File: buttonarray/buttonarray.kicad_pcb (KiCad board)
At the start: 2 copper layers, 0 parts

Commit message: add: component placement for numpad
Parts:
- added C1: 33pF, Capacitor_SMD:C_0201_0603Metric_Pad0.64x0.40mm_HandSolder, B.Cu at (55.9, 104.1)
- added C2: 1000uF, Capacitor_THT:CP_Radial_D13.0mm_P5.00mm, B.Cu at (50.8, 114.3)
- added C3: 100 uF, Capacitor_THT:CP_Radial_D6.3mm_P2.50mm, B.Cu at (76.2, 48.3)
- added C4: 330uF, Capacitor_THT:CP_Radial_D10.0mm_P5.00mm, B.Cu at (66.0, 50.8)
- added D1: 1N5819, Diode_THT:D_DO-41_SOD81_P10.16mm_Horizontal, B.Cu at (83.8, 53.3)
- added D10: 1N5819, Diode_THT:D_DO-41_SOD81_P10.16mm_Horizontal, B.Cu at (104.1, 94.0)
- added D11: 1N5819, Diode_THT:D_DO-41_SOD81_P10.16mm_Horizontal, B.Cu at (124.5, 94.0)
- added D12: 1N5819, Diode_THT:D_DO-41_SOD81_P10.16mm_Horizontal, B.Cu at (144.8, 94.0)
- added D13: 1N5819, Diode_THT:D_DO-41_SOD81_P10.16mm_Horizontal, B.Cu at (83.8, 114.3)
- added D14: 1N5819, Diode_THT:D_DO-41_SOD81_P10.16mm_Horizontal, B.Cu at (104.1, 114.3)
- added D15: 1N5819, Diode_THT:D_DO-41_SOD81_P10.16mm_Horizontal, B.Cu at (124.5, 114.3)
- added D16: 1N5819, Diode_THT:D_DO-41_SOD81_P10.16mm_Horizontal, B.Cu at (147.3, 114.3)
- added D17: 1N5819, Diode_THT:D_DO-41_SOD81_P10.16mm_Horizontal, B.Cu at (61.0, 40.6)
- added D2: 1N5819, Diode_THT:D_DO-41_SOD81_P10.16mm_Horizontal, B.Cu at (104.1, 53.3)
- added D3: 1N5819, Diode_THT:D_DO-41_SOD81_P10.16mm_Horizontal, B.Cu at (124.5, 53.3)
- added D4: 1N5819, Diode_THT:D_DO-41_SOD81_P10.16mm_Horizontal, B.Cu at (144.8, 53.3)
- added D5: 1N5819, Diode_THT:D_DO-41_SOD81_P10.16mm_Horizontal, B.Cu at (83.8, 73.7)
- added D6: 1N5819, Diode_THT:D_DO-41_SOD81_P10.16mm_Horizontal, B.Cu at (104.1, 73.7)
- added D7: 1N5819, Diode_THT:D_DO-41_SOD81_P10.16mm_Horizontal, B.Cu at (124.5, 73.7)
- added D8: 1N5819, Diode_THT:D_DO-41_SOD81_P10.16mm_Horizontal, B.Cu at (144.8, 73.7)
- added D9: 1N5819, Diode_THT:D_DO-41_SOD81_P10.16mm_Horizontal, B.Cu at (83.8, 94.0)
- added GPIOEXP1: mcp23016, Mission_DMX_Footprint_Library:mcp23016, F.Cu at (62.2, 118.1)
- added J1: CtrlPins, Connector_IDC:IDC-Header_2x08_P2.54mm_Latch_Vertical, B.Cu at (53.3, 73.7)
- added L1: 330 uH, Inductor_SMD:L_Fastron_PISN_Handsoldering, B.Cu at (71.1, 33.0)
- added Q1: 2N2219, Package_TO_SOT_THT:TO-39-3, B.Cu at (157.5, 33.0)
- added Q10: 2N2219, Package_TO_SOT_THT:TO-39-3, B.Cu at (96.5, 33.0)
- added Q11: 2N2219, Package_TO_SOT_THT:TO-39-3, B.Cu at (170.2, 71.1)
- added Q12: 2N2219, Package_TO_SOT_THT:TO-39-3, B.Cu at (170.3, 114.3)
- added Q13: 2N2219, Package_TO_SOT_THT:TO-39-3, B.Cu at (116.8, 33.0)
- added Q14: 2N2219, Package_TO_SOT_THT:TO-39-3, B.Cu at (170.2, 50.8)
- added Q15: 2N2219, Package_TO_SOT_THT:TO-39-3, B.Cu at (94.0, 124.5)
- added Q16: 2N2219, Package_TO_SOT_THT:TO-39-3, B.Cu at (137.2, 33.0)
- added Q2: 2N2219, Package_TO_SOT_THT:TO-39-3, B.Cu at (78.7, 88.9)
- added Q3: 2N2219, Package_TO_SOT_THT:TO-39-3, B.Cu at (114.3, 124.5)
- added Q4: 2N2219, Package_TO_SOT_THT:TO-39-3, B.Cu at (78.7, 58.4)
- added Q5: 2N2219, Package_TO_SOT_THT:TO-39-3, B.Cu at (78.7, 106.7)
- added Q6: 2N2219, Package_TO_SOT_THT:TO-39-3, B.Cu at (137.2, 124.5)
- added Q7: 2N2219, Package_TO_SOT_THT:TO-39-3, B.Cu at (78.7, 76.2)
- added Q8: 2N2219, Package_TO_SOT_THT:TO-39-3, B.Cu at (170.2, 91.4)
- added Q9: 2N2219, Package_TO_SOT_THT:TO-39-3, B.Cu at (154.9, 124.5)
- added R1: 10K, Resistor_SMD:R_0805_2012Metric_Pad1.20x1.40mm_HandSolder, B.Cu at (58.4, 99.1)
- added R10: 330 Ohm, Resistor_SMD:R_1206_3216Metric_Pad1.30x1.75mm_HandSolder, B.Cu at (104.1, 123.5)
- added R11: 3K, Resistor_SMD:R_1206_3216Metric_Pad1.30x1.75mm_HandSolder, B.Cu at (68.6, 61.0)
- added R12: 3K, Resistor_SMD:R_1206_3216Metric_Pad1.30x1.75mm_HandSolder, B.Cu at (78.7, 114.3)
- added R13: 3K, Resistor_SMD:R_1206_3216Metric_Pad1.30x1.75mm_HandSolder, B.Cu at (127.0, 127.0)
- added R14: 330 Ohm, Resistor_SMD:R_1206_3216Metric_Pad1.30x1.75mm_HandSolder, B.Cu at (76.2, 66.0)
- added R15: 330 Ohm, Resistor_SMD:R_1206_3216Metric_Pad1.30x1.75mm_HandSolder, B.Cu at (73.7, 116.8)
- added R16: 330 Ohm, Resistor_SMD:R_1206_3216Metric_Pad1.30x1.75mm_HandSolder, B.Cu at (124.5, 121.9)
- added R17: 3K, Resistor_SMD:R_1206_3216Metric_Pad1.30x1.75mm_HandSolder, B.Cu at (68.6, 78.7)
- added R18: 3K, Resistor_SMD:R_1206_3216Metric_Pad1.30x1.75mm_HandSolder, B.Cu at (170.2, 99.1)
- added R19: 3K, Resistor_SMD:R_1206_3216Metric_Pad1.30x1.75mm_HandSolder, B.Cu at (144.8, 127.0)
- added R2: 10K, Resistor_SMD:R_0805_2012Metric_Pad1.20x1.40mm_HandSolder, B.Cu at (53.3, 99.1)
- added R20: 330 Ohm, Resistor_SMD:R_1206_3216Metric_Pad1.30x1.75mm_HandSolder, B.Cu at (68.6, 68.6)
- added R21: 330 Ohm, Resistor_SMD:R_1206_3216Metric_Pad1.30x1.75mm_HandSolder, B.Cu at (166.7, 83.8)
- added R22: 330 Ohm, Resistor_SMD:R_1206_3216Metric_Pad1.30x1.75mm_HandSolder, B.Cu at (142.2, 120.9)
- added R23: 3K, Resistor_SMD:R_1206_3216Metric_Pad1.30x1.75mm_HandSolder, B.Cu at (86.4, 35.6)
- added R24: 330 Ohm, Resistor_SMD:R_1206_3216Metric_Pad1.30x1.75mm_HandSolder, B.Cu at (83.8, 30.5)
- added R25: 3K, Resistor_SMD:R_1206_3216Metric_Pad1.30x1.75mm_HandSolder, B.Cu at (167.6, 78.7)
- added R26: 3K, Resistor_SMD:R_1206_3216Metric_Pad1.30x1.75mm_HandSolder, B.Cu at (167.7, 121.9)
- added R27: 330 Ohm, Resistor_SMD:R_1206_3216Metric_Pad1.30x1.75mm_HandSolder, B.Cu at (167.6, 63.5)
- added R28: 330 Ohm, Resistor_SMD:R_1206_3216Metric_Pad1.30x1.75mm_HandSolder, B.Cu at (167.7, 106.7)
- added R29: 3K, Resistor_SMD:R_1206_3216Metric_Pad1.30x1.75mm_HandSolder, B.Cu at (104.1, 30.5)
- added R3: 10K, Resistor_SMD:R_0805_2012Metric_Pad1.20x1.40mm_HandSolder, B.Cu at (48.3, 99.1)
- added R30: 330 Ohm, Resistor_SMD:R_1206_3216Metric_Pad1.30x1.75mm_HandSolder, B.Cu at (106.7, 34.6)
- added R31: 3K, Resistor_SMD:R_1206_3216Metric_Pad1.30x1.75mm_HandSolder, B.Cu at (167.6, 58.4)
- added R32: 3K, Resistor_SMD:R_1206_3216Metric_Pad1.30x1.75mm_HandSolder, B.Cu at (83.8, 125.5)
- added R33: 330 Ohm, Resistor_SMD:R_1206_3216Metric_Pad1.30x1.75mm_HandSolder, B.Cu at (167.6, 43.2)
- added R34: 330 Ohm, Resistor_SMD:R_1206_3216Metric_Pad1.30x1.75mm_HandSolder, B.Cu at (78.7, 121.9)
- added R35: 3K, Resistor_SMD:R_1206_3216Metric_Pad1.30x1.75mm_HandSolder, B.Cu at (124.5, 30.5)
- added R36: 330 Ohm, Resistor_SMD:R_1206_3216Metric_Pad1.30x1.75mm_HandSolder, B.Cu at (126.3, 35.6)
- added R4: 3.9K, Resistor_SMD:R_0603_1608Metric_Pad0.98x0.95mm_HandSolder, B.Cu at (50.8, 104.1)
- added R5: 3K, Resistor_SMD:R_1206_3216Metric_Pad1.30x1.75mm_HandSolder, B.Cu at (144.8, 30.5)
- added R6: 3K, Resistor_SMD:R_1206_3216Metric_Pad1.30x1.75mm_HandSolder, B.Cu at (78.7, 96.5)
- added R7: 3K, Resistor_SMD:R_1206_3216Metric_Pad1.30x1.75mm_HandSolder, B.Cu at (119.4, 124.5)
- added R8: 330 Ohm, Resistor_SMD:R_1206_3216Metric_Pad1.30x1.75mm_HandSolder, B.Cu at (147.3, 35.6)
- added R9: 330 Ohm, Resistor_SMD:R_1206_3216Metric_Pad1.30x1.75mm_HandSolder, B.Cu at (73.7, 99.1)
- added SW1: SW_Push_LED, Mission_DMX_Footprint_Library:MX-1.0u-LED, F.Cu at (94.0, 48.3)
- added SW10: SW_Push_LED, Mission_DMX_Footprint_Library:MX-1.0u-LED, F.Cu at (114.3, 88.9)
- added SW11: SW_Push_LED, Mission_DMX_Footprint_Library:MX-1.0u-LED, F.Cu at (134.6, 88.9)
- added SW12: SW_Push_LED, Mission_DMX_Footprint_Library:MX-1.0u-LED, F.Cu at (154.9, 88.9)
- added SW13: SW_Push_LED, Mission_DMX_Footprint_Library:MX-1.0u-LED, F.Cu at (94.0, 109.2)
- added SW14: SW_Push_LED, Mission_DMX_Footprint_Library:MX-1.0u-LED, F.Cu at (114.3, 109.2)
- added SW15: SW_Push_LED, Mission_DMX_Footprint_Library:MX-1.0u-LED, B.Cu at (134.6, 109.2)
- added SW16: SW_Push_LED, Mission_DMX_Footprint_Library:MX-1.0u-LED, F.Cu at (154.9, 109.2)
- added SW17: Addr_DIP_SW, Button_Switch_THT:SW_DIP_SPSTx03_Slide_9.78x9.8mm_W7.62mm_P2.54mm, F.Cu at (59.6, 94.0)
- added SW2: SW_Push_LED, Mission_DMX_Footprint_Library:MX-1.0u-LED, F.Cu at (114.3, 48.3)
- added SW3: SW_Push_LED, Mission_DMX_Footprint_Library:MX-1.0u-LED, F.Cu at (134.6, 48.3)
- added SW4: SW_Push_LED, Mission_DMX_Footprint_Library:MX-1.0u-LED, F.Cu at (154.9, 48.3)
- added SW5: SW_Push_LED, Mission_DMX_Footprint_Library:MX-1.0u-LED, F.Cu at (94.0, 68.6)
- added SW6: SW_Push_LED, Mission_DMX_Footprint_Library:MX-1.0u-LED, F.Cu at (114.3, 68.6)
- added SW7: SW_Push_LED, Mission_DMX_Footprint_Library:MX-1.0u-LED, F.Cu at (134.6, 68.6)
- added SW8: SW_Push_LED, Mission_DMX_Footprint_Library:MX-1.0u-LED, F.Cu at (154.9, 68.6)
- added SW9: SW_Push_LED, Mission_DMX_Footprint_Library:MX-1.0u-LED, F.Cu at (94.0, 88.9)
- added U1: LM2575-3.3BT, Package_TO_SOT_THT:TO-220-5_Vertical, B.Cu at (55.9, 33.0)

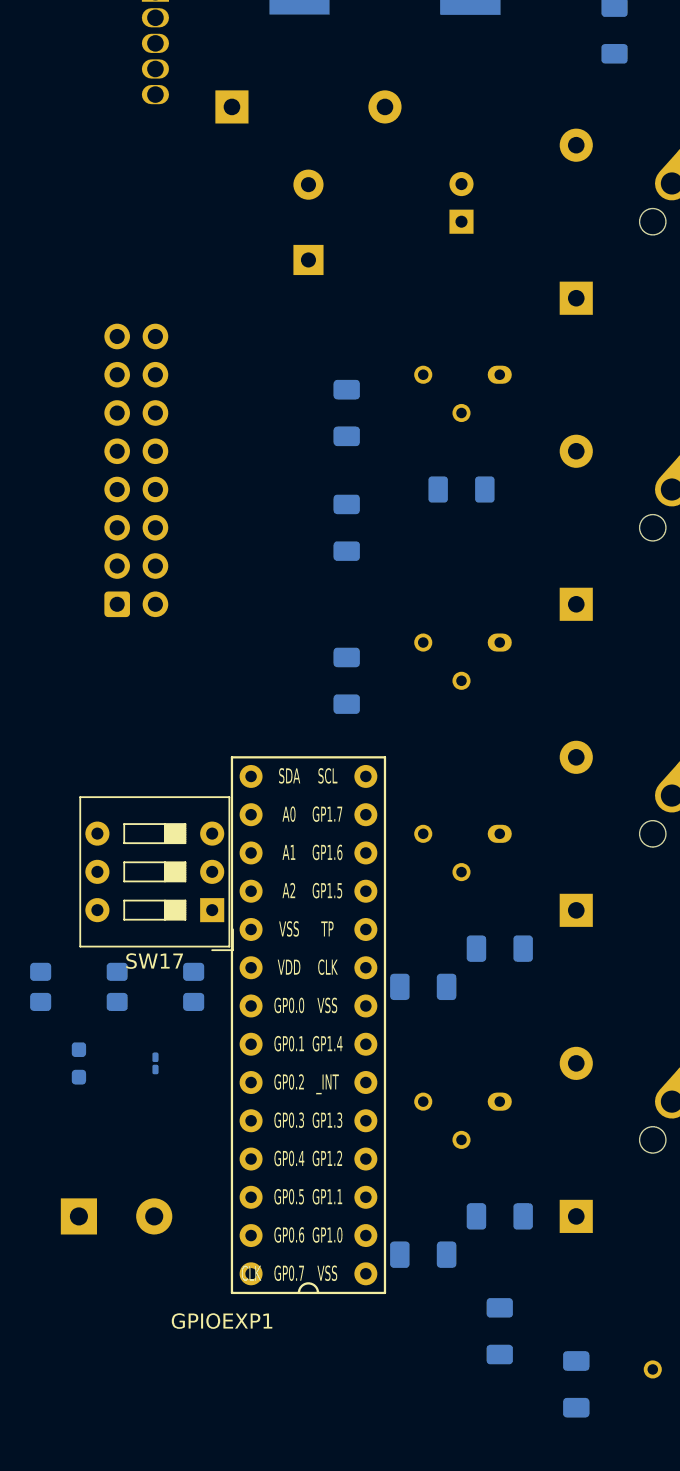
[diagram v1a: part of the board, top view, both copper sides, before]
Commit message: chg: component text positions
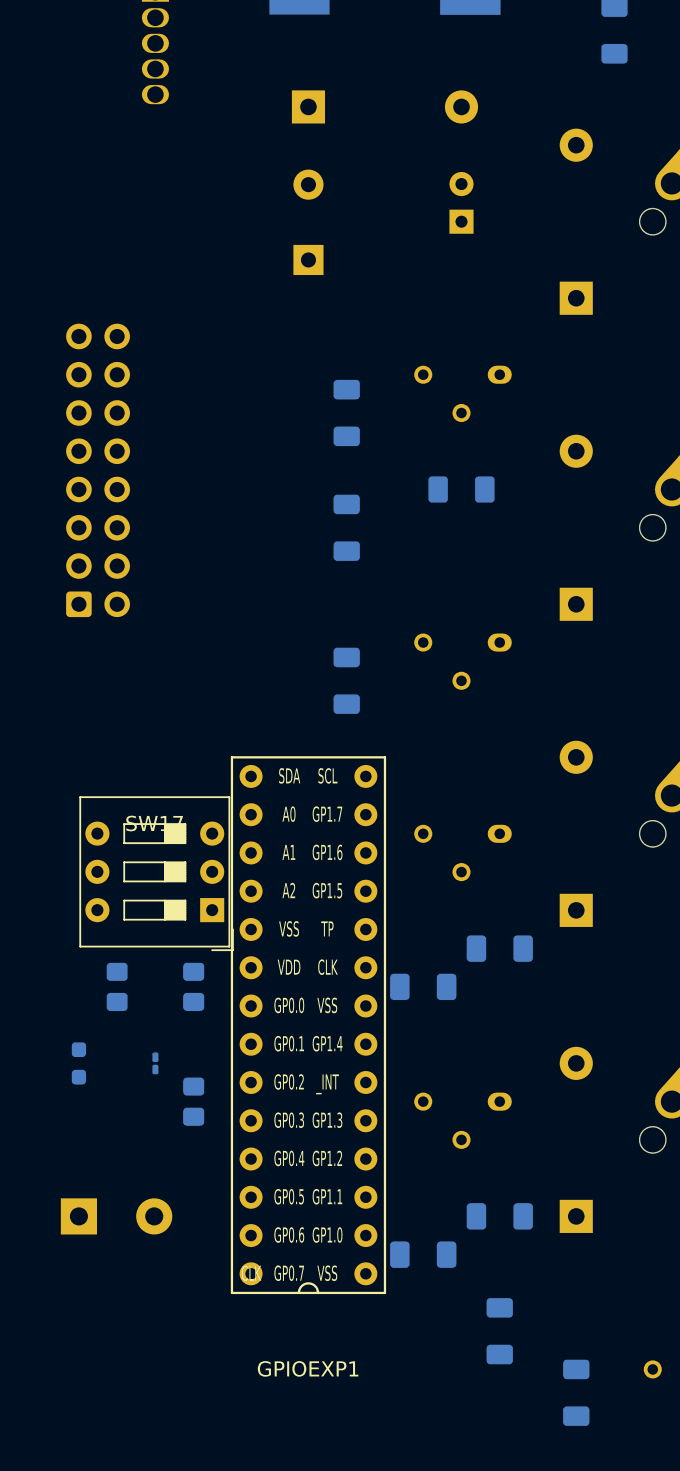
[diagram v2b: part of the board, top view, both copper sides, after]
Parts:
- moved R3 12.7 mm to (58.4, 106.7)
- moved R23 5.68 mm to (83.8, 30.5)
- moved R24 5.68 mm to (86.4, 35.6)
- moved D17 5.08 mm to (66.0, 40.6)
- moved J1 2.54 mm to (50.8, 73.7)
- moved R32 0.56 mm to (83.8, 126.0)

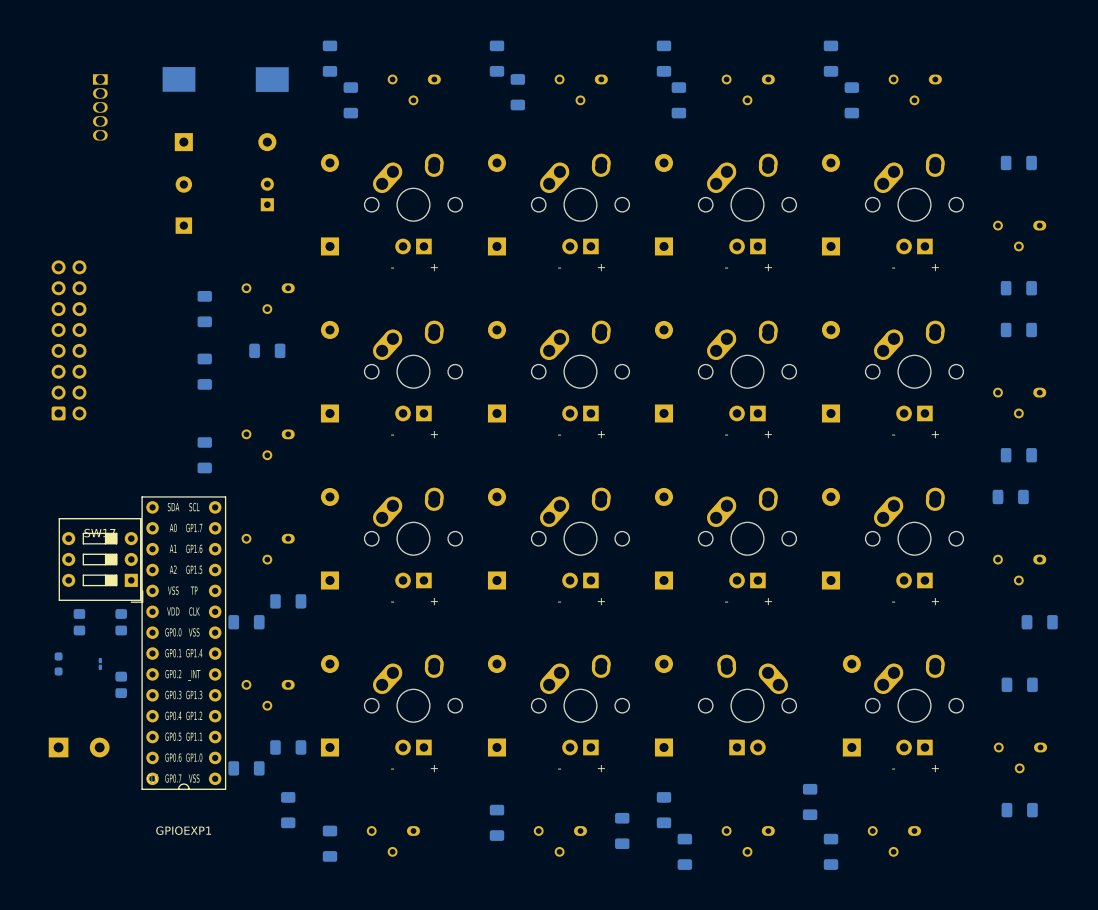
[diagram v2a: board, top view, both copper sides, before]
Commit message: add: numpad routing prototype
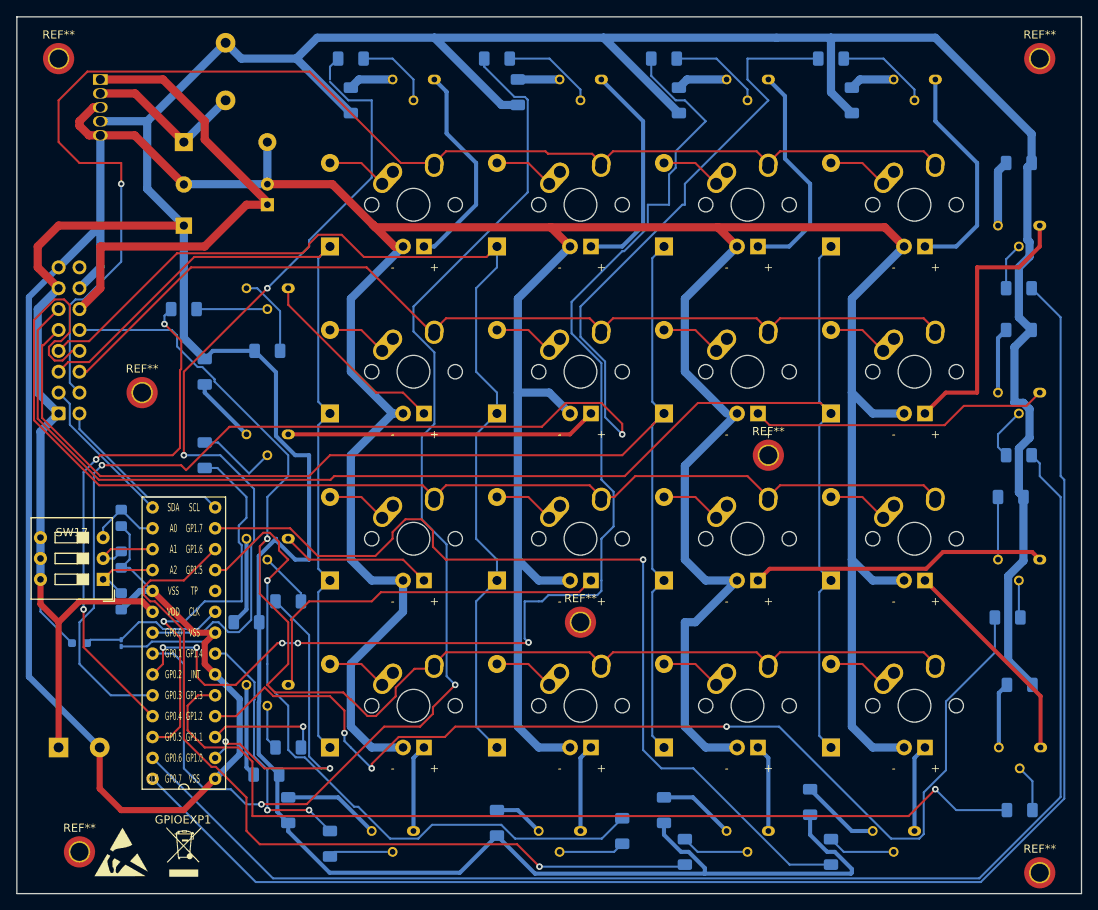
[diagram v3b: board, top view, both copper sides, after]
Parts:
- added REF**: MountingHole_2.2mm_M2_DIN965_Pad_TopOnly, MountingHole:MountingHole_2.2mm_M2_DIN965_Pad_TopOnly, F.Cu at (170.2, 30.5)
- added REF**: MountingHole_2.2mm_M2_DIN965_Pad_TopOnly, MountingHole:MountingHole_2.2mm_M2_DIN965_Pad_TopOnly, F.Cu at (61.0, 71.1)
- added REF**: MountingHole_2.2mm_M2_DIN965_Pad_TopOnly, MountingHole:MountingHole_2.2mm_M2_DIN965_Pad_TopOnly, F.Cu at (170.2, 129.5)
- added REF**: MountingHole_2.2mm_M2_DIN965_Pad_TopOnly, MountingHole:MountingHole_2.2mm_M2_DIN965_Pad_TopOnly, F.Cu at (50.8, 30.5)
- added REF**: ESD-Logo_6.6x6mm_SilkScreen, Symbol:ESD-Logo_6.6x6mm_SilkScreen, F.Cu at (58.4, 127.0)
- added REF**: MountingHole_2.2mm_M2_DIN965_Pad_TopOnly, MountingHole:MountingHole_2.2mm_M2_DIN965_Pad_TopOnly, F.Cu at (53.3, 127.0)
- added REF**: MountingHole_2.2mm_M2_DIN965_Pad_TopOnly, MountingHole:MountingHole_2.2mm_M2_DIN965_Pad_TopOnly, F.Cu at (114.3, 99.1)
- added REF**: WEEE-Logo_4.2x6mm_SilkScreen, Symbol:WEEE-Logo_4.2x6mm_SilkScreen, F.Cu at (66.0, 127.0)
- added REF**: MountingHole_2.2mm_M2_DIN965_Pad_TopOnly, MountingHole:MountingHole_2.2mm_M2_DIN965_Pad_TopOnly, F.Cu at (137.2, 78.7)
- L1: footprint Inductor_SMD:L_Fastron_PISN_Handsoldering -> Inductor_THT:L_Radial_D12.5mm_P7.00mm_Fastron_09HCP
- SW15: moved to F.Cu
- moved R3 20.3 mm to (58.4, 86.4)
- moved R2 9.16 mm to (58.4, 91.4)
- moved R18 3.95 mm to (166.3, 98.5), turned to 0 degrees
- moved R4 3.59 mm to (53.3, 101.6), turned to 0 degrees
- moved C1 3.59 mm to (58.4, 101.6), turned to -90 degrees
- moved SW17 3.43 mm to (56.2, 93.8)
- moved R1 2.54 mm to (58.4, 96.5)
- moved R23 2.54 mm to (86.4, 30.5), turned to 0 degrees
- moved L1 2.54 mm to (71.1, 35.6), turned to 90 degrees
- moved D16 2.54 mm to (144.8, 114.3)
- moved R11 2.54 mm to (66.0, 61.0), turned to 0 degrees
- moved R15 2.54 mm to (76.1, 117.6)
- turned R14 to 0 degrees
- turned R25 to 180 degrees
- turned R29 to 0 degrees
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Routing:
- net GND: track 0.00 -> 628.2 mm
- net +3V3: track 0.00 -> 554.6 mm
- net LED8D: track 0.00 -> 184.1 mm
- net BTN_C4: track 0.00 -> 182.9 mm
- net LED4D: track 0.00 -> 172.2 mm, vias 0 -> 2
- net LED7D: track 0.00 -> 163.7 mm
- net BTN_R1: track 0.00 -> 161.6 mm, vias 0 -> 1
- net BTN_C3: track 0.00 -> 157.9 mm
- net BTN_R4: track 0.00 -> 154.2 mm, vias 0 -> 1
- net LED3D: track 0.00 -> 148.8 mm, vias 0 -> 5
- net BTN_R3: track 0.00 -> 147.9 mm
- net LED2D: track 0.00 -> 146.6 mm, vias 0 -> 2
- net LED11D: track 0.00 -> 132.1 mm, vias 0 -> 3
- net BTN_C2: track 0.00 -> 128.3 mm
- net LED12D: track 0.00 -> 117.2 mm, vias 0 -> 1
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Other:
- board outline added: 129.5 x 106.7 mm

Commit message: fix: drill distances
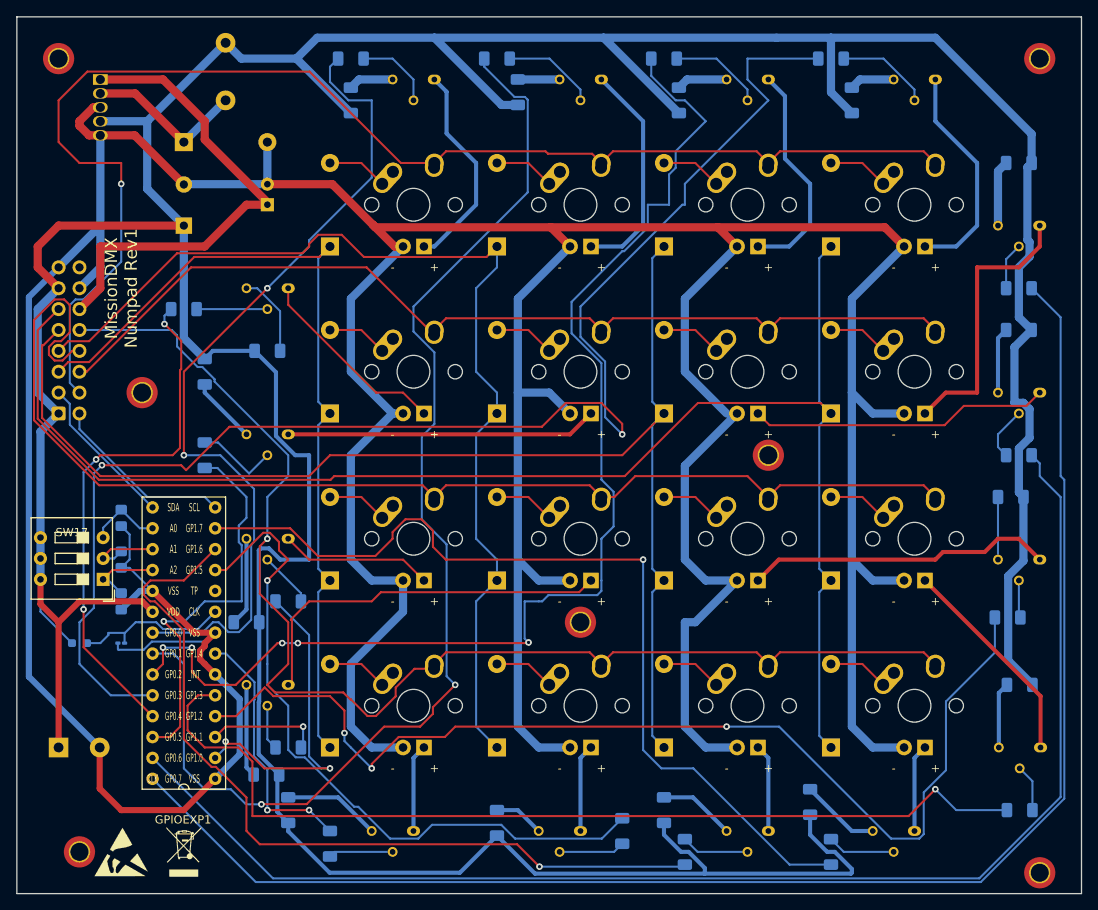
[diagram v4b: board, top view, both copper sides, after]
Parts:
- REF** (x6): value MountingHole_2.2mm_M2_DIN965_Pad_TopOnly -> M2
- turned C1 to 180 degrees
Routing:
- net Net-(C1-Pad1): track 17.9 -> 19.8 mm
- net GND: track 628.2 -> 630.0 mm
- net LED11: track 36.1 -> 37.4 mm
- net +3V3: track 554.6 -> 554.0 mm
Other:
- board text added: "MissionDMX Numpad Rev1"

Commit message: fix: missing ground plane
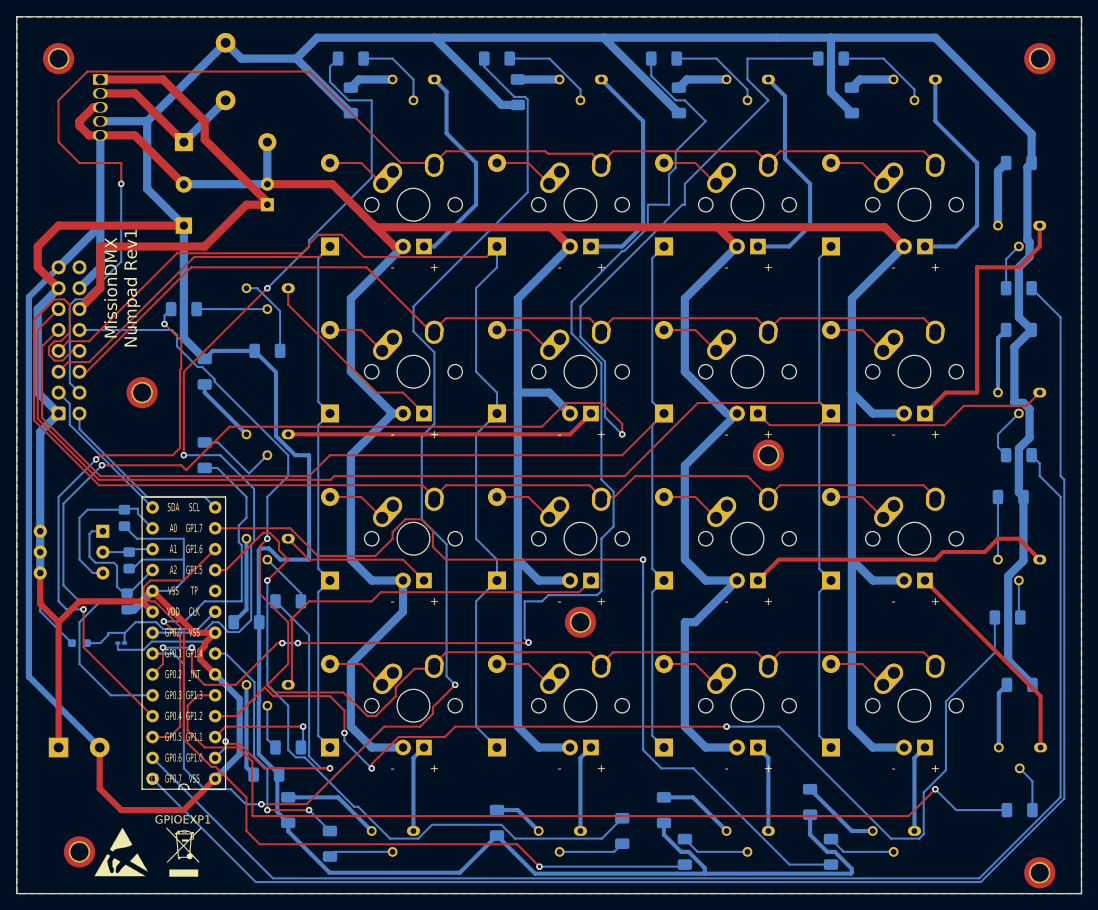
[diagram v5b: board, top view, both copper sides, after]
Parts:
- SW17: moved to B.Cu
- moved SW17 5.85 mm to (56.2, 88.0)
- moved R2 0.97 mm to (59.4, 91.5)
- moved R1 0.72 mm to (59.1, 96.5)
- moved R3 0.39 mm to (58.8, 86.4)
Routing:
- net GND: track 630.0 -> 642.9 mm
- net Net-(GPIOEXP1-Pad16): track 9.07 -> 19.3 mm
- net Net-(GPIOEXP1-Pad18): track 9.38 -> 17.7 mm
- net LED4D: track 172.2 -> 177.4 mm
- net LED5D: track 64.3 -> 68.0 mm
- net Net-(GPIOEXP1-Pad17): track 9.44 -> 6.72 mm
- net +3V3: track 554.0 -> 554.9 mm
- added copper zone on F.Cu, net +3V3
- added copper zone on B.Cu, net GND
